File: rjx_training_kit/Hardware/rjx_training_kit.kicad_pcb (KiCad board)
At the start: 4 copper layers, 100 x 100 mm, 110 parts, among them J1 Barrel_Jack_Switch, J2 Conn_01x32_Pin, J3 Conn_01x32_Pin, J4 LiPo_4.2V, J5 LiPo_4.2V, J6 CHG_OUT, J7 CAN_Bus, J8 CAN_Bus, J9 Conn_01x03_Pin, Q1 BC817, Q2 BC817, Q3 BC817, Q4 BC808, Q5 BC817, SW1 SW_Push, SW2 SW_Push, U1 TLV76133DCY, U2 LD39200DPUR, U3 BQ24072RGT, U4 LIS3DH, U5 BQ27441-G1, U6 KCSA02-136, U7 TMP1075DGK, U8 MCP2562-E-SN, U9 STM32L431RCTx, Y1 8MHz

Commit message: [RJX]: Rough component placement completion.
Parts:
- moved U6 136.6 mm to (71.0, 67.0)
- moved R30 136.2 mm to (51.9, 65.9)
- moved Q4 135.6 mm to (55.9, 66.7)
- moved R29 132.4 mm to (51.9, 67.8)
- moved JP2 127.9 mm to (47.0, 73.0)
- moved R24 127.6 mm to (62.2, 65.4)
- moved R28 122.8 mm to (62.2, 70.5)
- moved R23 122.5 mm to (62.2, 68.6)
- moved R25 122.4 mm to (62.2, 63.5)
- moved R27 119.3 mm to (79.8, 64.1), turned to 180 degrees
- moved R26 115.2 mm to (79.8, 66.0), turned to 180 degrees
- moved R22 112.4 mm to (79.8, 69.8), turned to 180 degrees
- moved R21 111.8 mm to (79.8, 67.9), turned to 180 degrees
- moved H3 104.6 mm to (43.2, 114.9)
- moved H4 94.9 mm to (130.2, 114.9)
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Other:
- board size 100 x 100 mm -> 97.5 x 88.6 mm

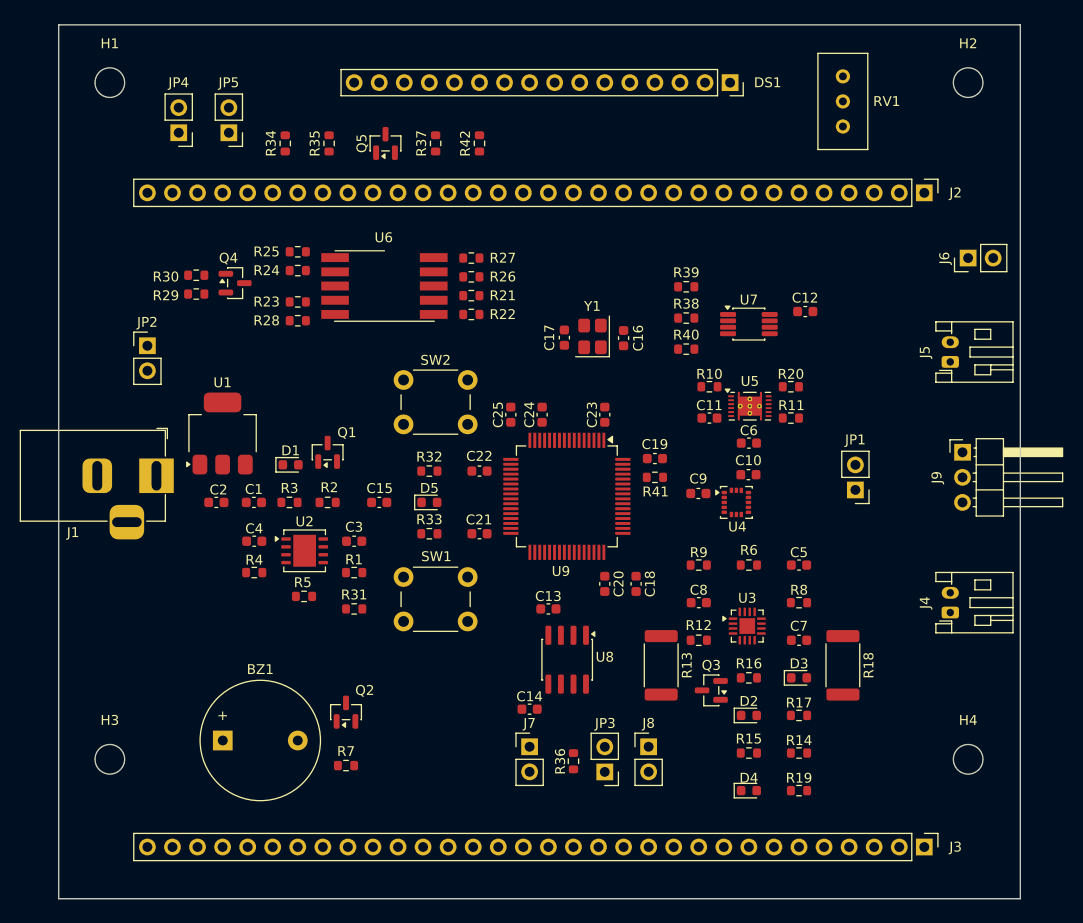
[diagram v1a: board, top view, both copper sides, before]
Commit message: [RJX]: Defined custom board outline.
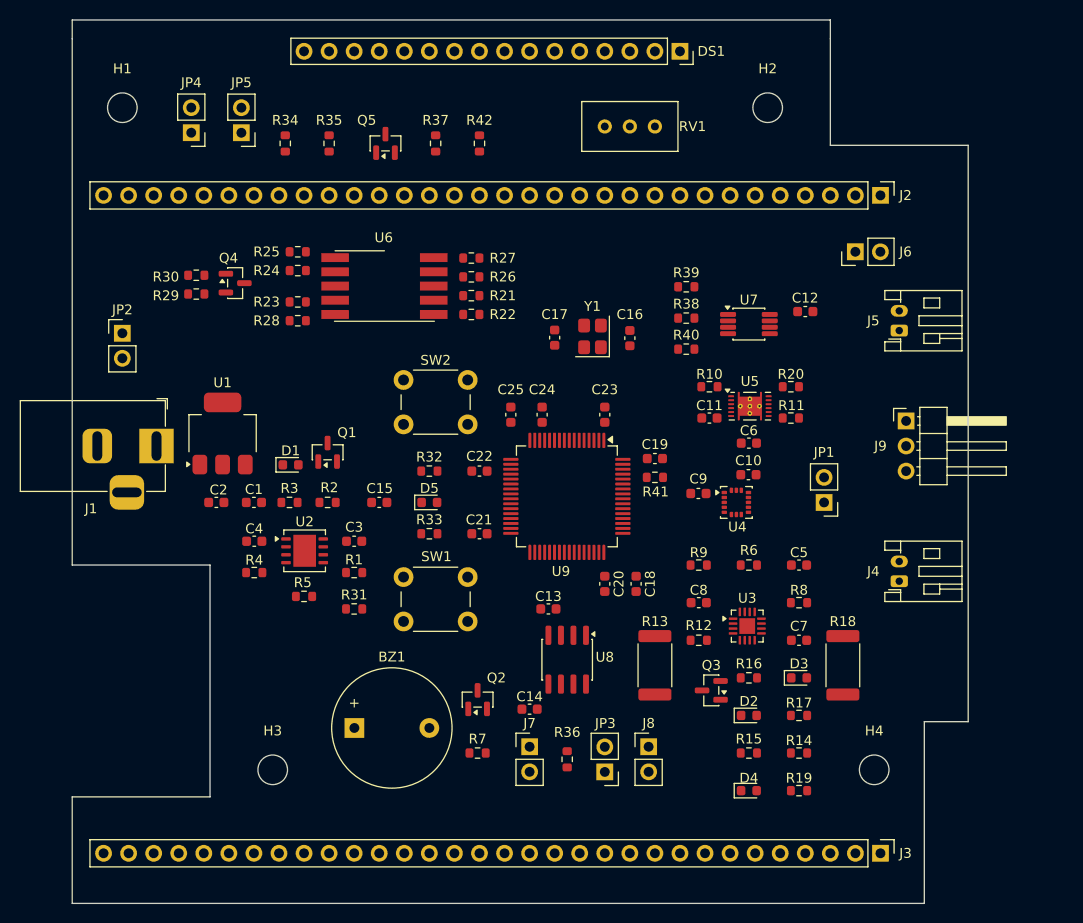
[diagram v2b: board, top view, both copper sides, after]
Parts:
- moved RV1 24.1 mm to (93.3, 50.8), turned to 180 degrees
- moved H2 20.5 mm to (109.9, 48.9)
- moved H3 16.5 mm to (59.7, 116.0)
- moved BZ1 13.4 mm to (68.0, 111.8)
- moved Q2 13.4 mm to (80.5, 108.9)
- moved R7 13.4 mm to (80.5, 114.3)
- moved J6 11.4 mm to (118.7, 63.5)
- moved H4 9.58 mm to (120.7, 116.0)
- moved J9 6.54 mm to (123.9, 80.6)
- moved J4 6.07 mm to (123.2, 96.9)
- moved J5 6.07 mm to (123.2, 71.5)
- moved DS1 5.99 mm to (101.0, 43.2)
- moved J3 4.49 mm to (121.3, 124.5)
- moved J2 4.45 mm to (121.3, 57.8)
- moved JP1 3.42 mm to (115.6, 88.9)
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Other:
- board size 97.5 x 88.6 mm -> 90.8 x 89.5 mm

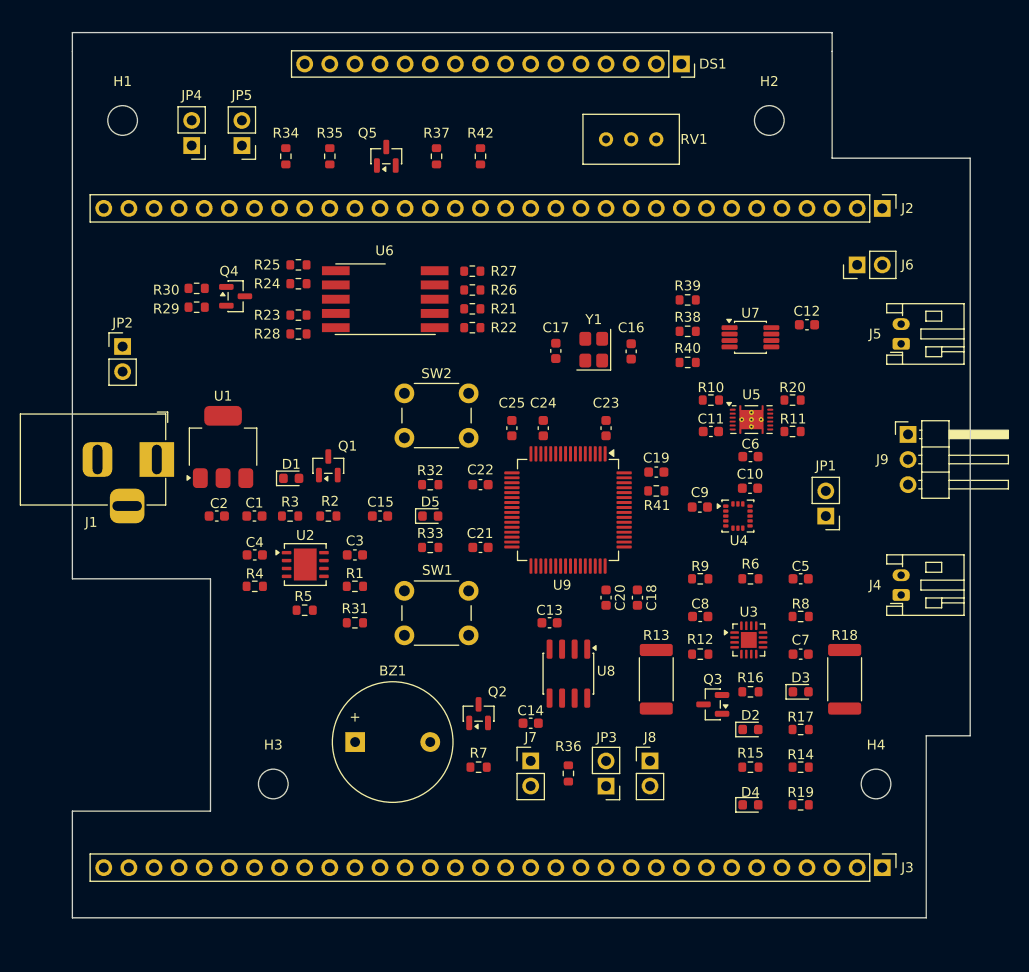
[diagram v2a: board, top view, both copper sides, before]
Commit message: [RJX]: Rounded edges for board's outline.
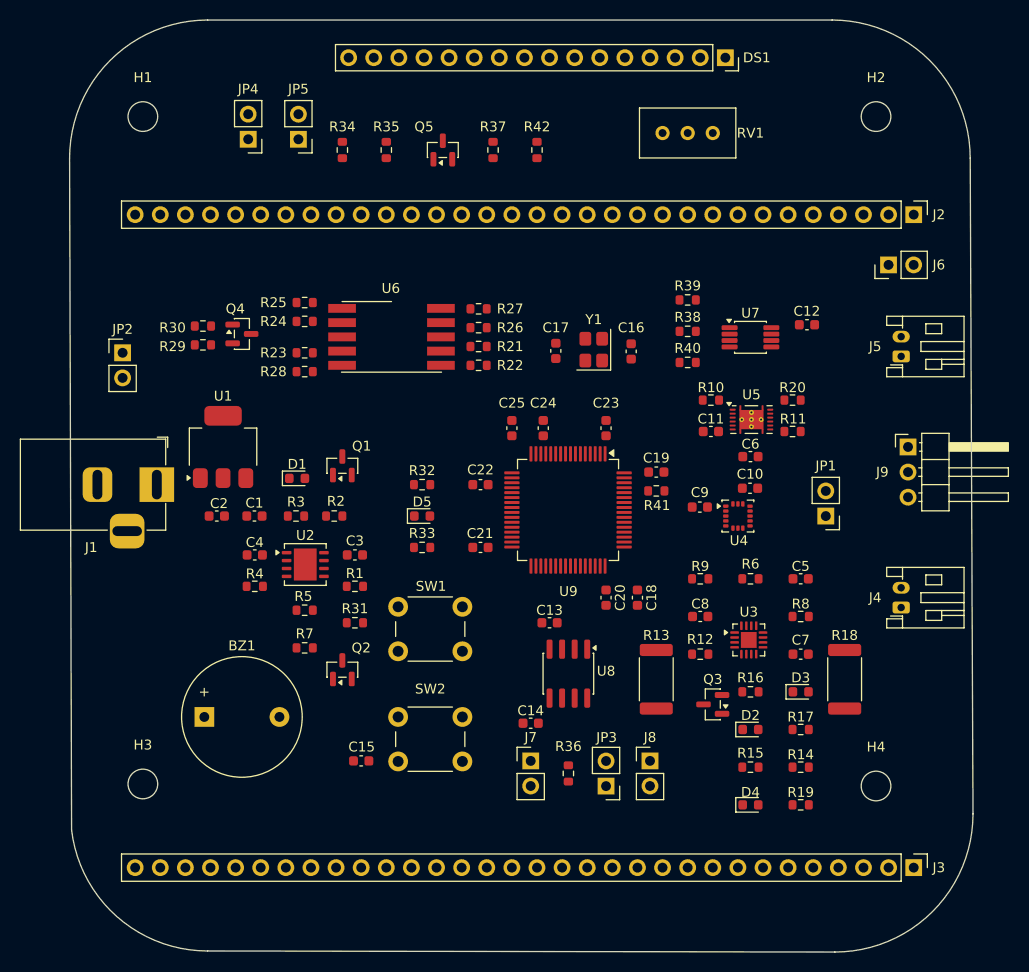
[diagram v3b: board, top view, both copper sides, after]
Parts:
- moved SW2 32.7 mm to (72.3, 109.2)
- moved C15 24.8 mm to (68.6, 113.7)
- moved R7 21.3 mm to (62.9, 102.2)
- moved BZ1 15.5 mm to (52.7, 109.2)
- moved Q2 14.5 mm to (66.7, 104.4)
- moved H3 13.2 mm to (46.5, 116.0)
- moved H2 10.8 mm to (120.7, 48.5)
- moved R35 5.75 mm to (71.1, 51.9)
- moved R37 5.75 mm to (81.9, 51.9)
- moved R42 5.75 mm to (86.4, 51.9)
- moved RV1 5.75 mm to (99.1, 50.2)
- moved JP5 5.75 mm to (62.2, 50.8)
- moved JP4 5.75 mm to (57.1, 50.8)
- moved R34 5.75 mm to (66.7, 51.9)
- moved Q5 5.75 mm to (76.8, 51.9)
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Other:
- board size 90.8 x 89.5 mm -> 91.4 x 94.3 mm
